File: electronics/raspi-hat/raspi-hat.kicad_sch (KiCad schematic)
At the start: 0 parts

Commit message: Add MAX33012EASA+ component to electronics/libraries/
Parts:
- added U?: MCP2517FD-xSL, Package_SO:SOIC-14_3.9x8.7mm_P1.27mm, symbol Interface_CAN_LIN:MCP2517FD-xSL
- added U?: MAX33012EASA+, 21-0041-3-M_90-0096-8L_MXM, symbol MAX33012EASA+:MAX33012EASA+
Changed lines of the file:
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@@
 (kicad_sch (version 20210621) (generator eeschema)
   (paper "A4")
-  (symbol_instances)
+  (symbol (lib_id "MAX33012EASA+:MAX33012EASA+") (at 135.89 62.23 0) (unit 1)
+    (in_bom yes) (on_board yes) (fields_autoplaced)
+    (property "Reference" "U?" (id 0) (at 156.21 52.6825 0)
+      (effects (font (size 1.524 1.524)))
+    )
+    (property "Value" "MAX33012EASA+" (id 1) (at 156.21 55.9615 0)
+      (effects (font (size 1.524 1.524)))
+    )
+    (property "Footprint" "21-0041-3-M_90-0096-8L_MXM" (id 2) (at 156.21 56.134 0)
+      (effects (font (size 1.524 1.524)) hide)
+    )
+    (property "Datasheet" "" (id 3) (at 135.89 62.23 0)
+      (effects (font (size 1.524 1.524)))
+    )
+    (pin "1")
+    (pin "2")
+    (pin "3")
+    (pin "4")
+    (pin "5")
+    (pin "6")
+    (pin "7")
+    (pin "8")
+  )
+  (symbol (lib_id "Interface_CAN_LIN:MCP2517FD-xSL") (at 104.14 67.31 0) (unit 1)
+    (in_bom yes) (on_board yes) (fields_autoplaced)
+    (property "Reference" "U?" (id 0) (at 104.14 50.3894 0))
+    (property "Value" "MCP2517FD-xSL" (id 1) (at 104.14 53.1645 0))
+    (property "Footprint" "Package_SO:SOIC-14_3.9x8.7mm_P1.27mm" (id 2) (at 104.14 92.71 0)
+      (effects (font (size 1.27 1.27)) hide)
+    )
+    (property "Datasheet" "https://ww1.microchip.com/downloads/en/DeviceDoc/20005688A.pdf" (id 3) (at 104.14 60.96 0)
+      (effects (font (size 1.27 1.27)) hide)
+    )
+    (pin "1")
+    (pin "10")
+    (pin "11")
+    (pin "12")
+    (pin "13")
+    (pin "14")
+    (pin "2")
+    (pin "3")
+    (pin "4")
+    (pin "5")
+    (pin "6")
+    (pin "7")
+    (pin "8")
+    (pin "9")
+  )
+  (sheet_instances
+    (path "/" (page "1"))
+  )
+  (symbol_instances
+    (path "/619d431d-b66a-45c2-a17a-a20c44728e7f"
+      (reference "U?") (unit 1) (value "MCP2517FD-xSL") (footprint "Package_SO:SOIC-14_3.9x8.7mm_P1.27mm")
+    )
+    (path "/b3440e58-ef45-4355-8334-c5e50597c83d"
+      (reference "U?") (unit 1) (value "MAX33012EASA+") (footprint "21-0041-3-M_90-0096-8L_MXM")
+    )
+  )
 )

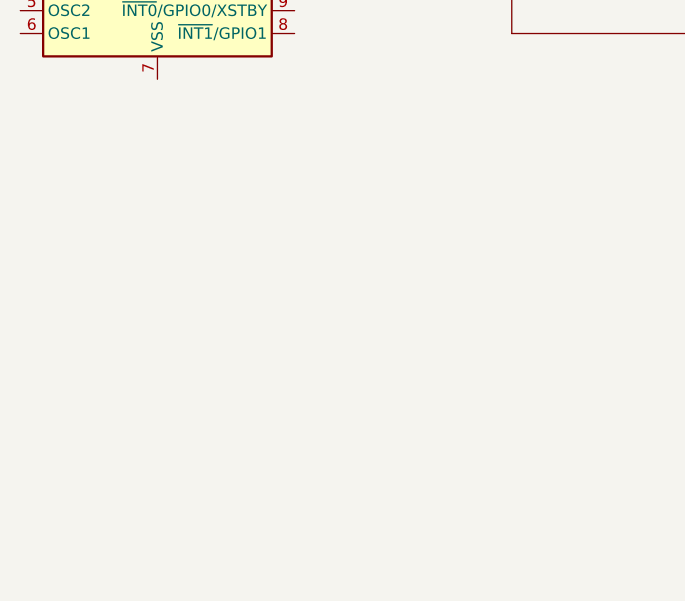
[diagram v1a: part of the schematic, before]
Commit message: Add components necessary for raspi hat
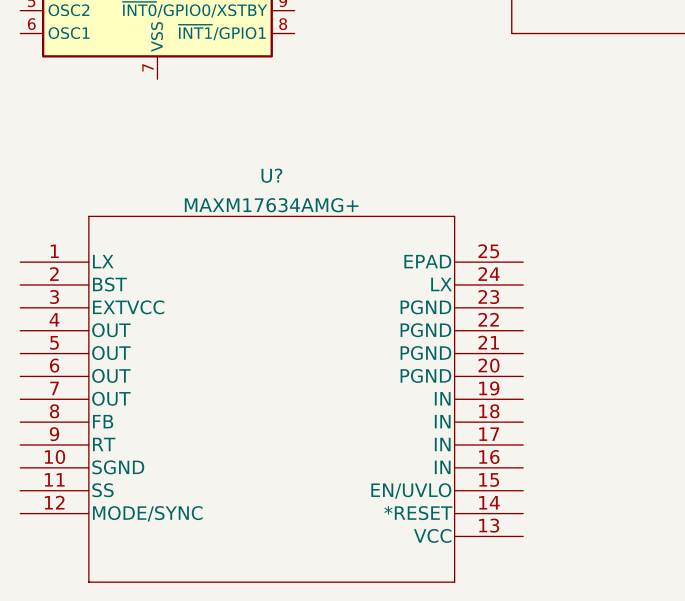
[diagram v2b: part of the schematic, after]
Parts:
- added U?: MAXM17634AMG+, 21-100342_M244A4+1_MXM, symbol MAXM17634AMG+:MAXM17634AMG+
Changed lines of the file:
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@@
+    (pin "9")
+  )
+  (symbol (lib_id "MAXM17634AMG+:MAXM17634AMG+") (at 88.9 100.33 0) (unit 1)
+    (in_bom yes) (on_board yes) (fields_autoplaced)
+    (property "Reference" "U?" (id 0) (at 116.84 90.7825 0)
+      (effects (font (size 1.524 1.524)))
+    )
+    (property "Value" "MAXM17634AMG+" (id 1) (at 116.84 94.0615 0)
+      (effects (font (size 1.524 1.524)))
+    )
+    (property "Footprint" "21-100342_M244A4+1_MXM" (id 2) (at 116.84 94.234 0)
+      (effects (font (size 1.524 1.524)) hide)
+    )
+    (property "Datasheet" "" (id 3) (at 88.9 100.33 0)
+      (effects (font (size 1.524 1.524)))
+    )
+    (pin "1")
+    (pin "10")
+    (pin "11")
+    (pin "12")
+    (pin "13")
+    (pin "14")
+    (pin "15")
+    (pin "16")
+    (pin "17")
+    (pin "18")
+    (pin "19")
+    (pin "2")
+    (pin "20")
+    (pin "21")
+    (pin "22")
+    (pin "23")
+    (pin "24")
+    (pin "25")
+    (pin "3")
+    (pin "4")
+    (pin "5")
+    (pin "6")
+    (pin "7")
+    (pin "8")
     (pin "9")
   )
@@
   )
   (symbol_instances
+    (path "/56d43536-30c6-4f11-bfeb-e9a5c87c3dfd"
+      (reference "U?") (unit 1) (value "MAXM17634AMG+") (footprint "21-100342_M244A4+1_MXM")
+    )
     (path "/619d431d-b66a-45c2-a17a-a20c44728e7f"
       (reference "U?") (unit 1) (value "MCP2517FD-xSL") (footprint "Package_SO:SOIC-14_3.9x8.7mm_P1.27mm")

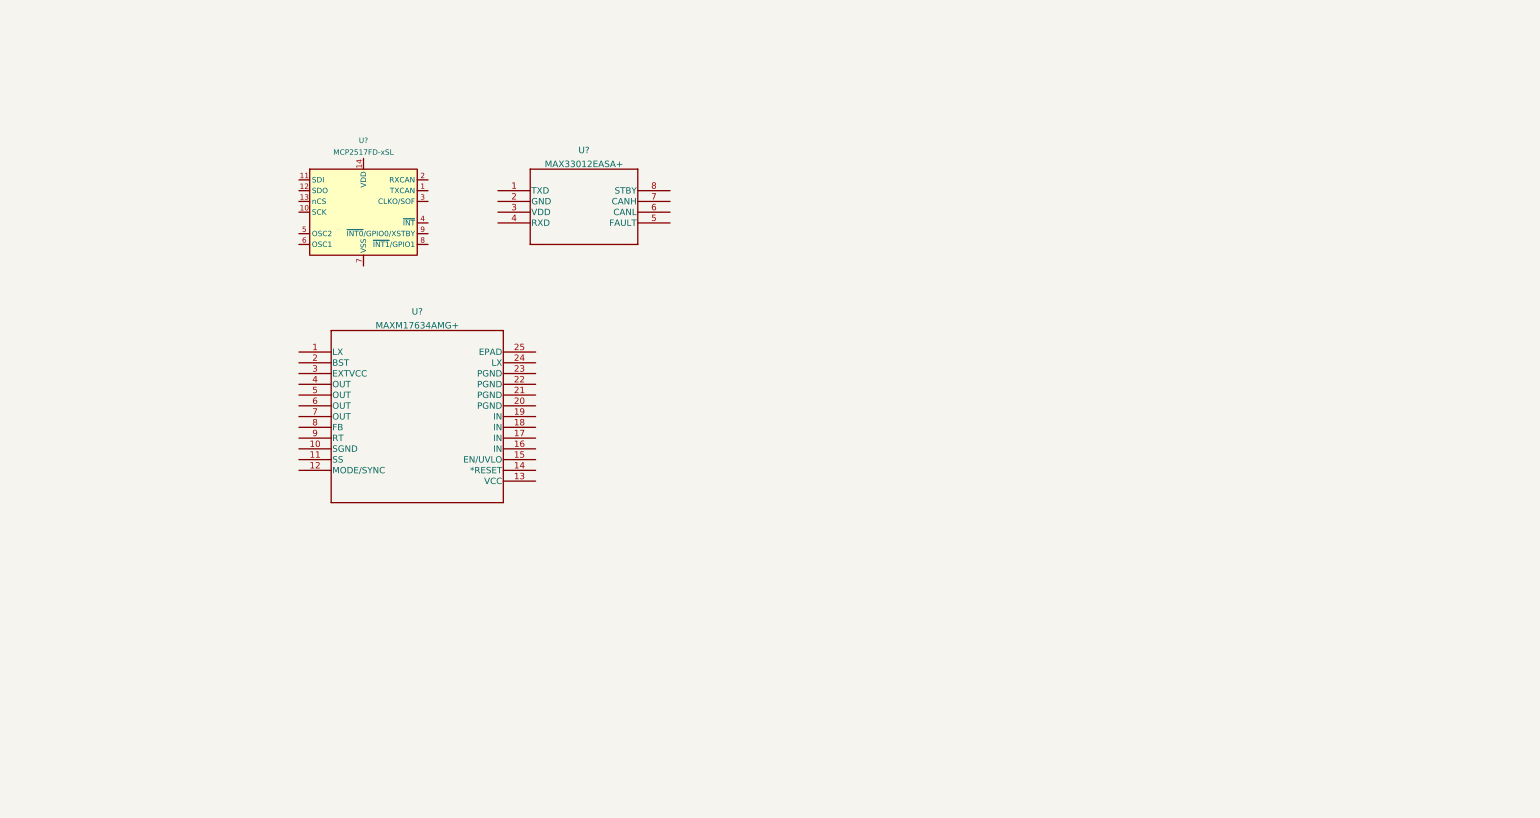
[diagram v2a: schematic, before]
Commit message: Add MYSGK02506BRSR and start adding MYMGA5R04RELA5RA to Raspi HAT
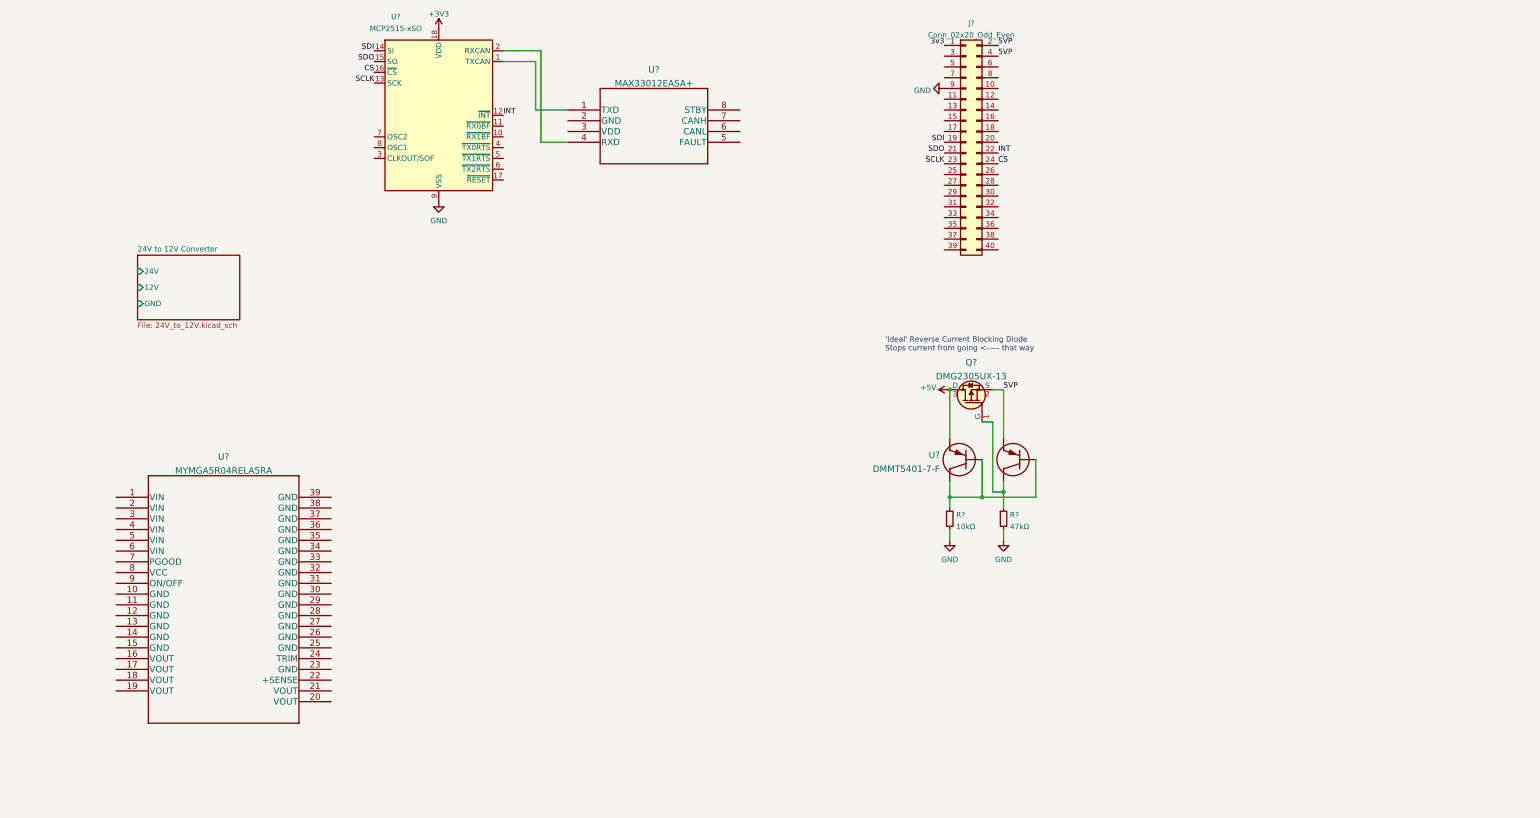
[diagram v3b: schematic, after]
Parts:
- removed U?: MAXM17634AMG+, 21-100342_M244A4+1_MXM, symbol MAXM17634AMG+:MAXM17634AMG+
- removed U?: MCP2517FD-xSL, Package_SO:SOIC-14_3.9x8.7mm_P1.27mm, symbol Interface_CAN_LIN:MCP2517FD-xSL
- added J?: Conn_02x20_Odd_Even, symbol Connector_Generic:Conn_02x20_Odd_Even
- added Q?: DMG2305UX-13, digikey-footprints:SOT-23-3, symbol dk_Transistors-FETs-MOSFETs-Single:DMG2305UX-13
- added R?: 10kΩ, symbol Device:R_Small
- added R?: 47kΩ, symbol Device:R_Small
- added U?: MYMGA5R04RELA5RA, MYMGA5R04RELA5RA_MUR, symbol MYMGA5R04RELA5RA:MYMGA5R04RELA5RA
- added U?: MCP2515-xSO, Package_SO:SOIC-18W_7.5x11.6mm_P1.27mm, symbol Interface_CAN_LIN:MCP2515-xSO
- added U?: DMMT5401-7-F, SOT_5401-7-F_DIO, symbol DMMT5401-7-F:DMMT5401-7-F
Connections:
- net at U?.1 (TXD): now also U?.1 (TXCAN)
- net at U?.4 (RXD): now also U?.2 (RXCAN)
- new net: R?.1, U?.2 (B1), U?.3 (B2), U?.4 (C2)
- new net: Q?.1 (G), R?.1, U?.1 (C1)
- new net +3V3: U?.18 (VDD)
- new net +5V: Q?.3 (D), U?.5 (E2)
- new net 3v3: J?.1 (Pin_1)
- new net 5VP: J?.2 (Pin_2), J?.4 (Pin_4), Q?.2 (S), U?.6 (E1)
- new net CS: J?.24 (Pin_24), U?.16 (~{CS})
- new net GND: J?.9 (Pin_9), R?.2, R?.2, U?.9 (VSS)
- new net INT: J?.22 (Pin_22), U?.12 (~{INT})
- new net SCLK: J?.23 (Pin_23), U?.13 (SCK)
- new net SDI: J?.19 (Pin_19), U?.14 (SI)
- new net SDO: J?.21 (Pin_21), U?.15 (SO)
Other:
- added sheet 24V to 12V Converter (24V_to_12V.kicad_sch)
- note added: "'Ideal' Reverse Current Blocking Diode Stops current from going <----- that way"
- moved on the sheet: U?

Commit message: Finish adding MYMGA5R04RELA5RA
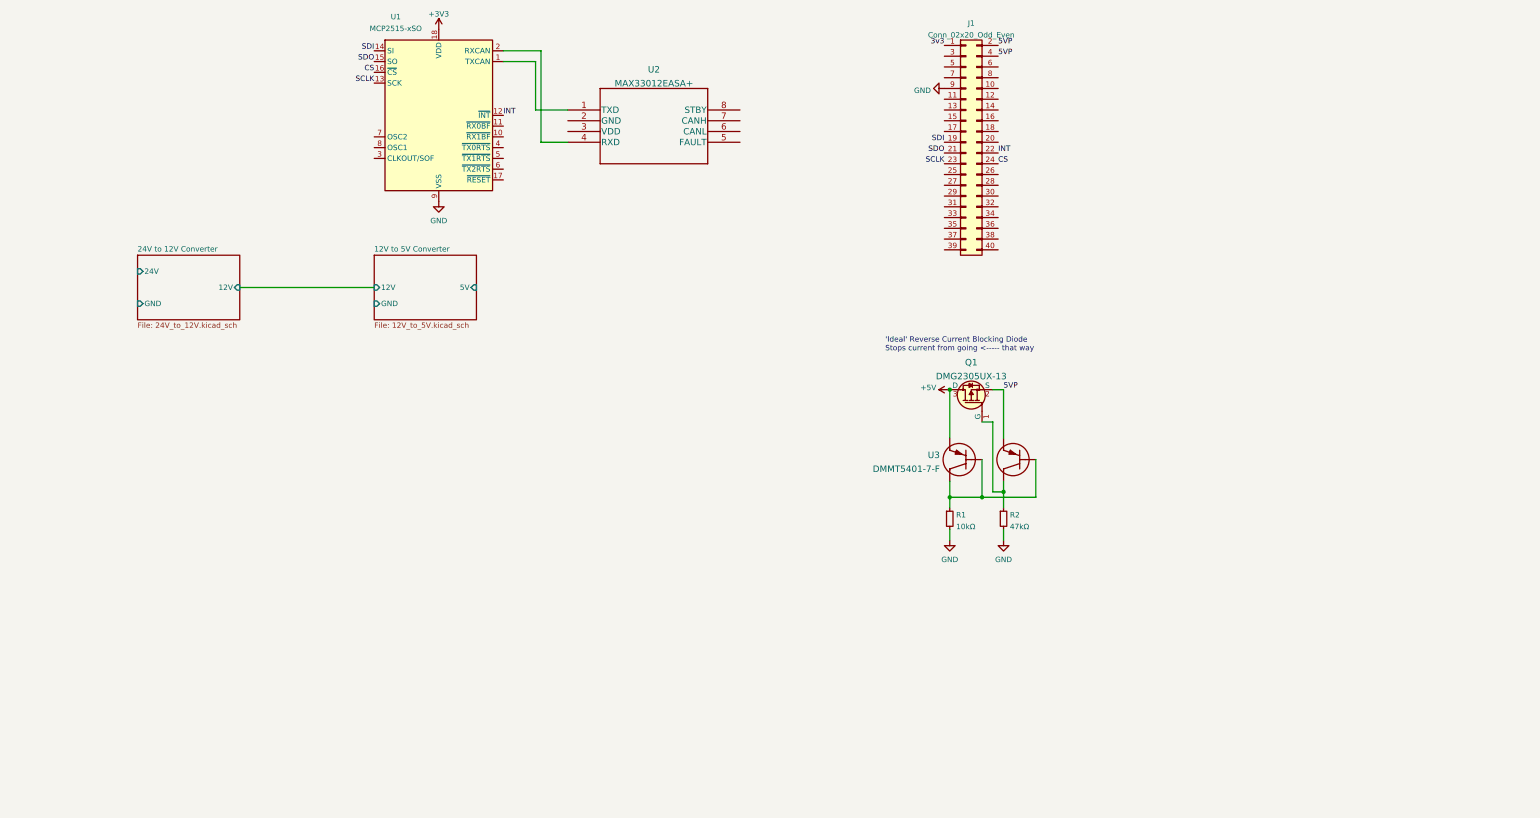
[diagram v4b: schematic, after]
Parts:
- removed U?: MYMGA5R04RELA5RA, MYMGA5R04RELA5RA_MUR, symbol MYMGA5R04RELA5RA:MYMGA5R04RELA5RA
- gave numbers to parts that had none: 7
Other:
- added sheet 12V to 5V Converter (12V_to_5V.kicad_sch)

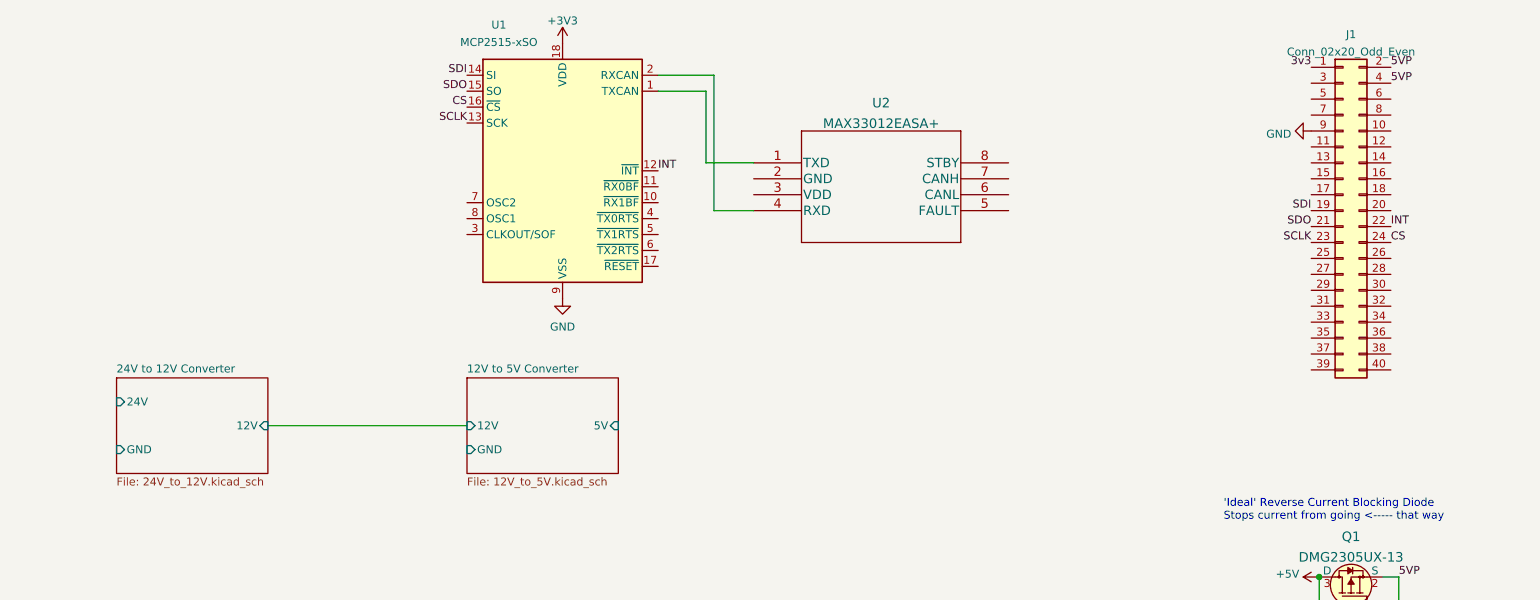
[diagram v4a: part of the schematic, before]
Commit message: Start laying out PCB for raspberry pi hat
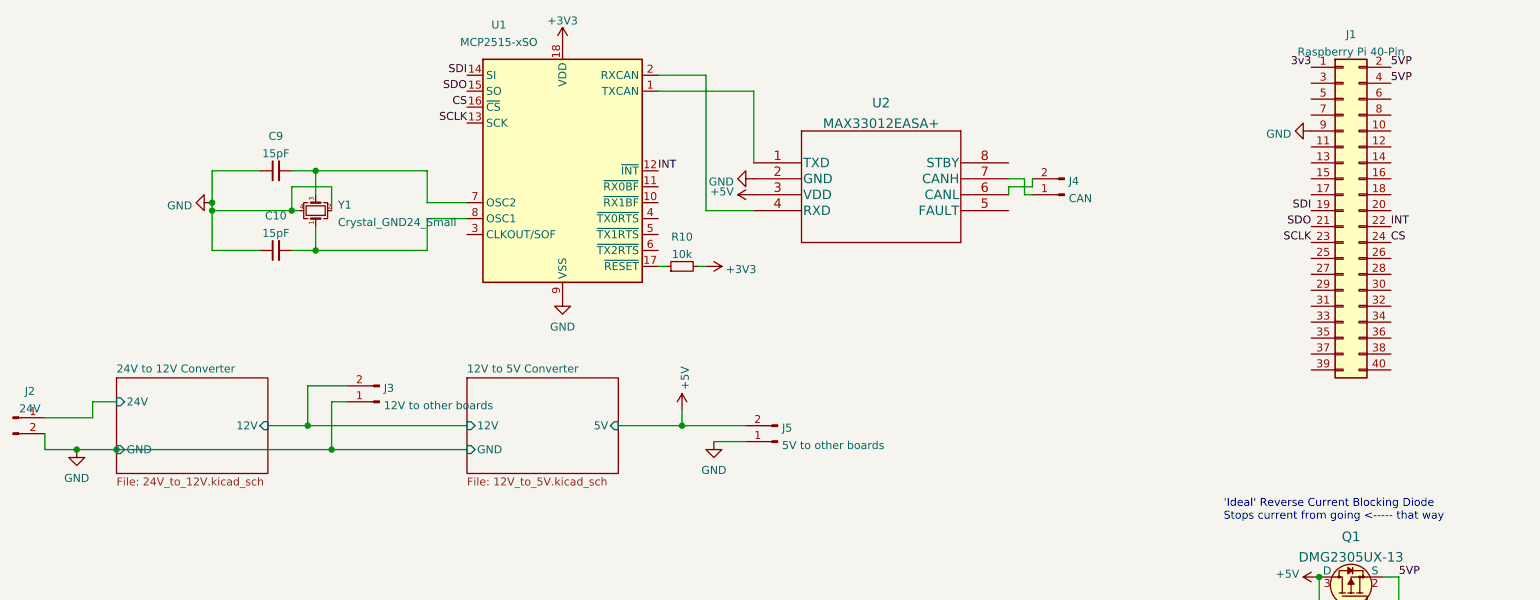
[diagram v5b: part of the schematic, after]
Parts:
- added C10, C9: 15pF, Capacitor_SMD:C_0603_1608Metric, symbol Device:C_Small
- added J2: 24V, Custom Footprints:PowerPoleThroughHole, symbol Connector:Conn_01x02_Male
- added J3: 12V to other boards, Custom Footprints:PowerPoleThroughHole, symbol Connector:Conn_01x02_Male
- added J4: CAN, Custom Footprints:LatchingConnector2POS, symbol Connector:Conn_01x02_Male
- added J5: 5V to other boards, Custom Footprints:LatchingConnector2POS, symbol Connector:Conn_01x02_Male
- added R10: 10k, Resistor_SMD:R_0603_1608Metric, symbol Device:R_Small
- added Y1: Crystal_GND24_Small, Crystal:Crystal_SMD_3225-4Pin_3.2x2.5mm, symbol Device:Crystal_GND24_Small
- J1: value Conn_02x20_Odd_Even -> Raspberry Pi 40-Pin; footprint (none) -> Connector_PinHeader_2.54mm:PinHeader_2x20_P2.54mm_Vertical
- R1, R2: footprint (none) -> Resistor_SMD:R_0603_1608Metric
- U2: footprint 21-0041-3-M_90-0096-8L_MXM -> MAX33012EASA+:MAX33012EASA+
- U3: footprint SOT_5401-7-F_DIO -> DMMT5401-7-F:DMMT5401-7-F
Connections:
- net +3V3: now also R10.2
- net +5V: now also U2.3 (VDD), J5.2 (Pin_2)
- net 12V to 5V Converter/12V: now also J3.2 (Pin_2)
- net 24V to 12V Converter/24V: now also J2.1 (Pin_1)
- net GND: now also U2.2 (GND), C10.1, C9.1, J2.2 (Pin_2), J3.1 (Pin_1), J5.1 (Pin_1), Y1.2, Y1.4
- net at U1.17 (~{RESET}): now also R10.1
- net at U1.7 (OSC2): now also C9.2, Y1.3
- net at U1.8 (OSC1): now also C10.2, Y1.1
- net at U2.6 (CANL): now also J4.2 (Pin_2)
- net at U2.7 (CANH): now also J4.1 (Pin_1)
